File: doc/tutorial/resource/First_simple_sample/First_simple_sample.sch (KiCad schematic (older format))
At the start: 3 parts, among them CN1 B2B-EH

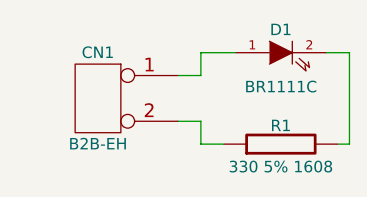
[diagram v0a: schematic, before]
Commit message: 最初のサンプルのチュートリアル作成中。
EHコネクタはKiCadにデフォルトでフットプリントがないので、
ヒロスギのピンヘッダに変更した。
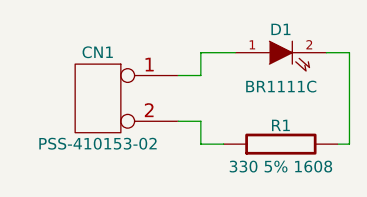
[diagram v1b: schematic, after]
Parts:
- CN1: value B2B-EH -> PSS-410153-02
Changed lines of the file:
@@
 LIBS:contrib
 LIBS:valves
+LIBS:First_simple_sample-cache
 EELAYER 27 0
 EELAYER END
@@
 Sheet 1 1
 Title ""
-Date "8 aug 2017"
+Date "9 aug 2017"
 Rev ""
 Comp ""
@@
 P 4250 3800
 F 0 "CN1" H 4250 4000 50  0000 C CNN
-F 1 "B2B-EH" H 4250 3600 50  0000 C CNN
+F 1 "PSS-410153-02" H 4250 3600 50  0000 C CNN
 F 2 "~" H 4250 3800 60  0000 C CNN
 F 3 "~" H 4250 3800 60  0000 C CNN
